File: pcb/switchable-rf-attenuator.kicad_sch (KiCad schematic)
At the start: 17 parts, among them J1 USB_B_Mini, J2 Conn_Coaxial, J3 Conn_Coaxial, SW1 SW_SPDT, U1 AS179-92LF, U2 AS179-92LF

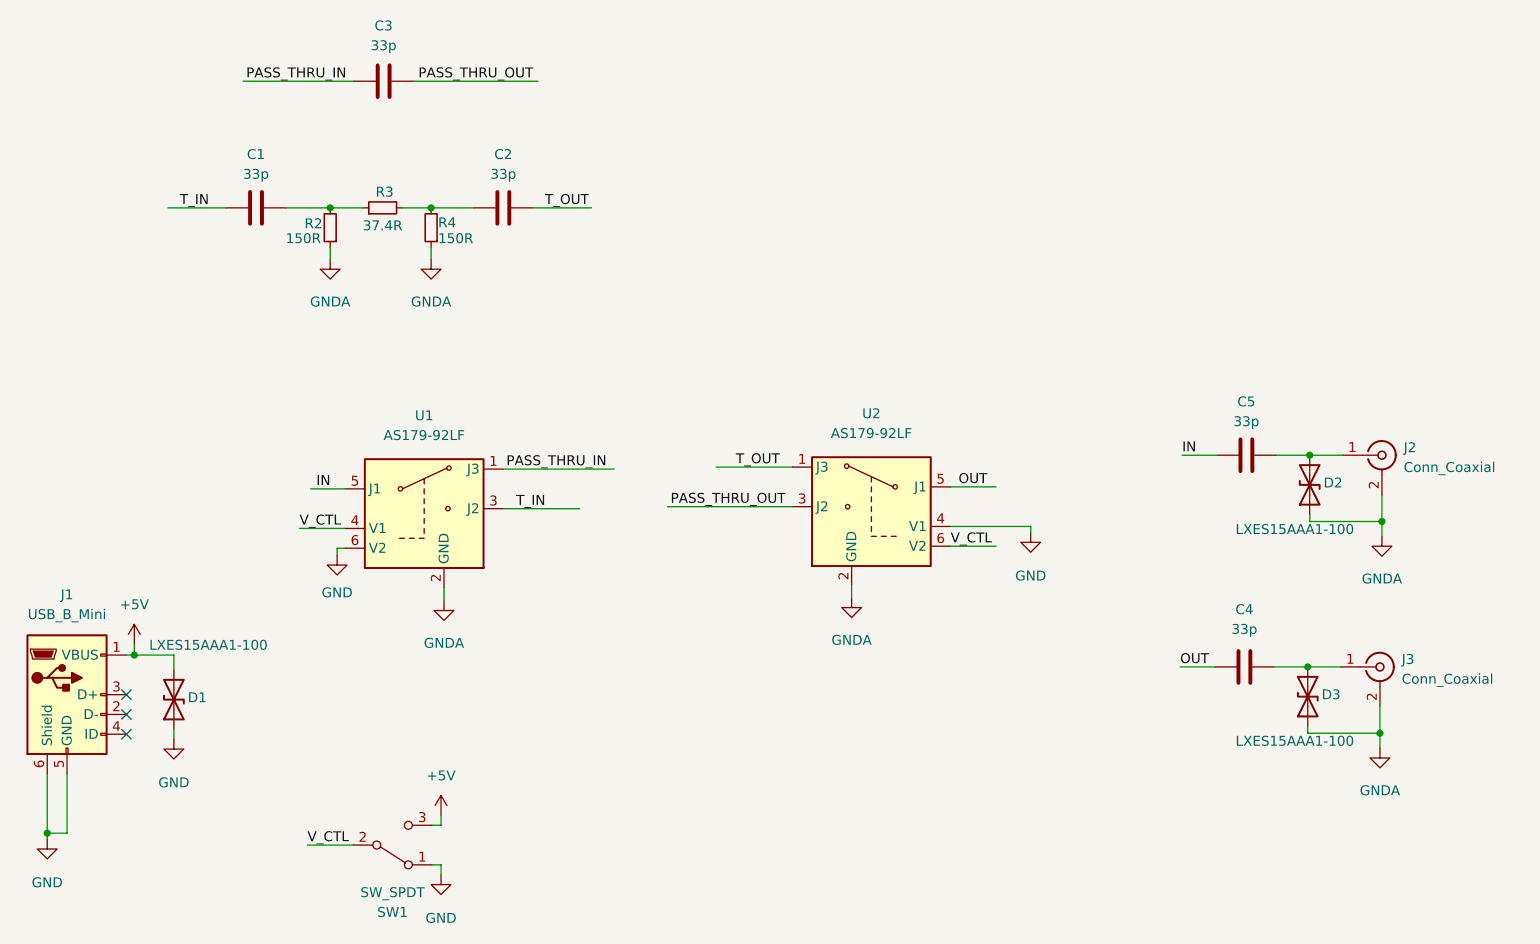
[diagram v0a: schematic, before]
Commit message: finish the trace routing
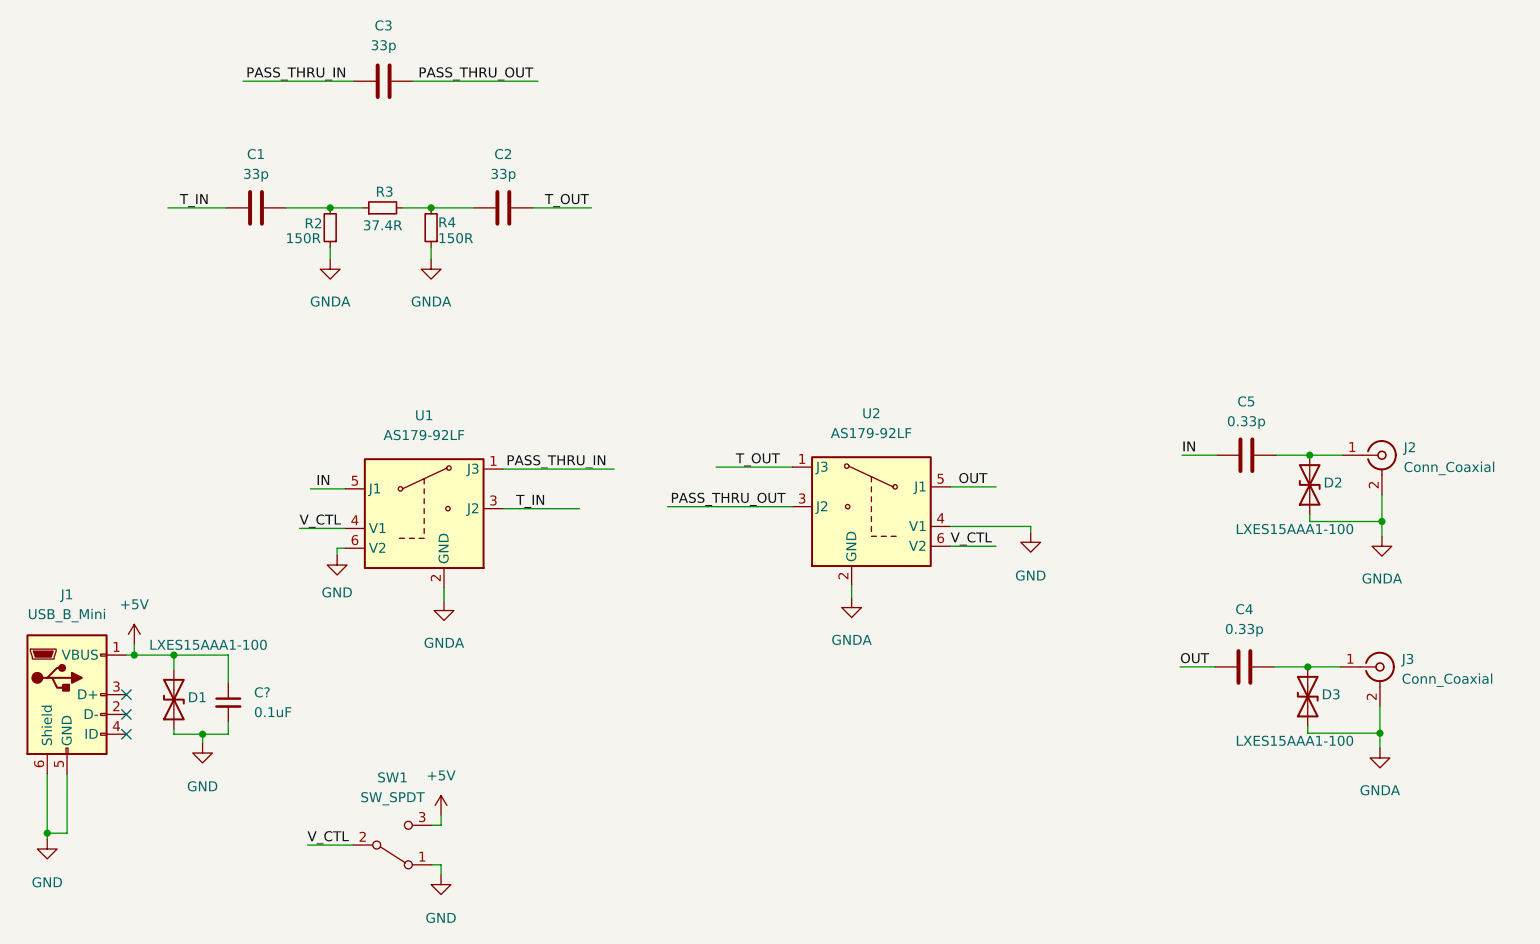
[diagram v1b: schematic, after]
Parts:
- added C?: 0.1uF, Capacitor_SMD:C_0805_2012Metric, symbol Device:C_Small
- C4, C5: value 33p -> 0.33p
- SW1: footprint Button_Switch_THT:SW_CuK_JS202011AQN_DPDT_Angled -> Button_Switch_SMD:SW_SPDT_CK-JS102011SAQN
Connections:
- net +5V: now also C?.1
- net GND: now also C?.2
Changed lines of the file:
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@@
   (junction (at 256.54 124.587) (diameter 0) (color 0 0 0 0)
   )
+  (junction (at 105.156 151.892) (diameter 0) (color 0 0 0 0)
+  )
   (junction (at 134.493 84.328) (diameter 0) (color 0 0 0 0)
   )
   (junction (at 96.393 141.732) (diameter 0) (color 0 0 0 0)
+  )
+  (junction (at 101.473 141.732) (diameter 0) (color 0 0 0 0)
   )
   (junction (at 247.015 143.256) (diameter 0) (color 0 0 0 0)
@@
     (stroke (width 0) (type default) (color 0 0 0 0))
   )
+  (wire (pts (xy 101.473 151.892) (xy 101.473 151.257))
+    (stroke (width 0) (type default) (color 0 0 0 0))
+  )
   (wire (pts (xy 95.377 141.732) (xy 96.393 141.732))
     (stroke (width 0) (type default) (color 0 0 0 0))
@@
     (stroke (width 0) (type default) (color 0 0 0 0))
   )
+  (wire (pts (xy 108.458 151.892) (xy 105.156 151.892))
+    (stroke (width 0) (type default) (color 0 0 0 0))
+  )
   (wire (pts (xy 118.618 166.116) (xy 124.46 166.116))
     (stroke (width 0) (type default) (color 0 0 0 0))
@@
     (stroke (width 0) (type default) (color 0 0 0 0))
   )
+  (wire (pts (xy 105.156 151.892) (xy 101.473 151.892))
+    (stroke (width 0) (type default) (color 0 0 0 0))
+  )
+  (wire (pts (xy 108.458 150.368) (xy 108.458 151.892))
+    (stroke (width 0) (type default) (color 0 0 0 0))
+  )
   (wire (pts (xy 134.493 84.328) (xy 139.954 84.328))
     (stroke (width 0) (type default) (color 0 0 0 0))
@@
     (stroke (width 0) (type default) (color 0 0 0 0))
   )
-  (wire (pts (xy 101.473 151.257) (xy 101.473 152.527))
+  (wire (pts (xy 105.156 153.035) (xy 105.156 151.892))
+    (stroke (width 0) (type default) (color 0 0 0 0))
+  )
+  (wire (pts (xy 108.458 141.732) (xy 108.458 145.288))
     (stroke (width 0) (type default) (color 0 0 0 0))
   )
@@
   )
   (wire (pts (xy 201.168 120.142) (xy 207.01 120.142))
+    (stroke (width 0) (type default) (color 0 0 0 0))
+  )
+  (wire (pts (xy 101.473 141.732) (xy 108.458 141.732))
     (stroke (width 0) (type default) (color 0 0 0 0))
   )
@@
   (symbol (lib_id "Switch:SW_SPDT") (at 129.54 166.116 0) (mirror x) (unit 1)
     (in_bom yes) (on_board yes) (fields_autoplaced)
-    (property "Reference" "SW1" (id 0) (at 129.54 174.752 0))
-    (property "Value" "SW_SPDT" (id 1) (at 129.54 172.212 0))
-    (property "Footprint" "Button_Switch_THT:SW_CuK_JS202011AQN_DPDT_Angled" (id 2) (at 129.54 166.116 0)
+    (property "Reference" "SW1" (id 0) (at 129.54 157.48 0))
+    (property "Value" "SW_SPDT" (id 1) (at 129.54 160.02 0))
+    (property "Footprint" "Button_Switch_SMD:SW_SPDT_CK-JS102011SAQN" (id 2) (at 129.54 166.116 0)
       (effects (font (size 1.27 1.27)) hide)
     )
@@
     (in_bom yes) (on_board yes) (fields_autoplaced)
     (property "Reference" "C5" (id 0) (at 239.141 109.22 90))
-    (property "Value" "33p" (id 1) (at 239.141 111.76 90))
+    (property "Value" "0.33p" (id 1) (at 239.141 111.76 90))
     (property "Footprint" "Capacitor_SMD:C_0805_2012Metric" (id 2) (at 242.951 115.1128 0)
       (effects (font (size 1.27 1.27)) hide)
@@
     (in_bom yes) (on_board yes) (fields_autoplaced)
     (property "Reference" "C4" (id 0) (at 238.887 135.89 90))
-    (property "Value" "33p" (id 1) (at 238.887 138.43 90))
+    (property "Value" "0.33p" (id 1) (at 238.887 138.43 90))
     (property "Footprint" "Capacitor_SMD:C_0805_2012Metric" (id 2) (at 242.697 142.2908 0)
       (effects (font (size 1.27 1.27)) hide)
@@
     (pin "2")
   )
-  (symbol (lib_id "power:GND") (at 101.473 152.527 0) (unit 1)
-    (in_bom yes) (on_board yes) (fields_autoplaced)
-    (property "Reference" "#PWR0113" (id 0) (at 101.473 158.877 0)
-      (effects (font (size 1.27 1.27)) hide)
-    )
-    (property "Value" "GND" (id 1) (at 101.473 158.115 0))
-    (property "Footprint" "" (id 2) (at 101.473 152.527 0)
-      (effects (font (size 1.27 1.27)) hide)
-    )
-    (property "Datasheet" "" (id 3) (at 101.473 152.527 0)
+  (symbol (lib_id "Device:C_Small") (at 108.458 147.828 0) (unit 1)
+    (in_bom yes) (on_board yes) (fields_autoplaced)
+    (property "Reference" "C?" (id 0) (at 111.76 146.5642 0)
+      (effects (font (size 1.27 1.27)) (justify left))
+    )
+    (property "Value" "0.1uF" (id 1) (at 111.76 149.1042 0)
+      (effects (font (size 1.27 1.27)) (justify left))
+    )
+    (property "Footprint" "Capacitor_SMD:C_0805_2012Metric" (id 2) (at 108.458 147.828 0)
+      (effects (font (size 1.27 1.27)) hide)
+    )
+    (property "Datasheet" "~" (id 3) (at 108.458 147.828 0)
+      (effects (font (size 1.27 1.27)) hide)
+    )
+    (pin "1")
+    (pin "2")
+  )
+  (symbol (lib_id "power:GND") (at 105.156 153.035 0) (unit 1)
+    (in_bom yes) (on_board yes) (fields_autoplaced)
+    (property "Reference" "#PWR0113" (id 0) (at 105.156 159.385 0)
+      (effects (font (size 1.27 1.27)) hide)
+    )
+    (property "Value" "GND" (id 1) (at 105.156 158.623 0))
+    (property "Footprint" "" (id 2) (at 105.156 153.035 0)
+      (effects (font (size 1.27 1.27)) hide)
+    )
+    (property "Datasheet" "" (id 3) (at 105.156 153.035 0)
       (effects (font (size 1.27 1.27)) hide)
     )
@@
     )
     (path "/5b668e57-1f4d-47b3-82ca-46fe5209da66"
-      (reference "C4") (unit 1) (value "33p") (footprint "Capacitor_SMD:C_0805_2012Metric")
+      (reference "C4") (unit 1) (value "0.33p") (footprint "Capacitor_SMD:C_0805_2012Metric")
     )
     (path "/58a3f0ab-965d-4148-8bd0-caba6d3ed17a"
-      (reference "C5") (unit 1) (value "33p") (footprint "Capacitor_SMD:C_0805_2012Metric")
+      (reference "C5") (unit 1) (value "0.33p") (footprint "Capacitor_SMD:C_0805_2012Metric")
+    )
+    (path "/8a8367a5-d8e2-4320-9281-c09c749f449f"
+      (reference "C?") (unit 1) (value "0.1uF") (footprint "Capacitor_SMD:C_0805_2012Metric")
     )
     (path "/a9264ea1-c27c-45dc-99bc-45e827b8b425"
@@
     )
     (path "/4f9b90bf-be15-44f8-a8d8-6eb9283f7320"
-      (reference "SW1") (unit 1) (value "SW_SPDT") (footprint "Button_Switch_THT:SW_CuK_JS202011AQN_DPDT_Angled")
+      (reference "SW1") (unit 1) (value "SW_SPDT") (footprint "Button_Switch_SMD:SW_SPDT_CK-JS102011SAQN")
     )
     (path "/23a34d8a-9387-4afb-a716-c3c7907c4eac"
